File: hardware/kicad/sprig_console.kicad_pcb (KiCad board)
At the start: 2 copper layers, 139.7 x 64.8 mm, 42 parts, among them J1 1020_battery_holder, SW1 W, SW2 A, SW3 S, SW4 D, SW5 I, SW6 J, SW7 K, SW8 L, SW9 Slideswitch, U1 Adafruit_TFT_ST7735, U2 MAX98357AETE+, U5 Pico, X1 Simple_Addon_v2

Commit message: updated PCB
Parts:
- moved SW9 19.2 mm to (179.7, 61.2)
- moved C4 16.5 mm to (176.5, 73.1), turned to -90 degrees
- moved D3 14.2 mm to (179.1, 73.4), turned to 90 degrees
- moved X1 9.53 mm to (184.1, 74.3)
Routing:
- net Net-(J1-Pin_4): track 72.4 -> 104.9 mm
- net Net-(D3-K): track 16.1 -> 37.8 mm
- net GND: track 20.1 -> 31.8 mm
- net +3V3: track 59.3 -> 66.4 mm
- net Net-(D3-A): track 5.38 -> 12.5 mm
- net unconnected-(SW9-A-Pad1): track 0.00 -> 5.46 mm
- net GPIO1: track 19.6 -> 25.0 mm
- net GPIO0: track 14.3 -> 18.2 mm, vias 0 -> 1
- net GPIO3: track 12.8 -> 11.2 mm
- net GPIO2: track 13.4 -> 13.3 mm, vias 0 -> 2

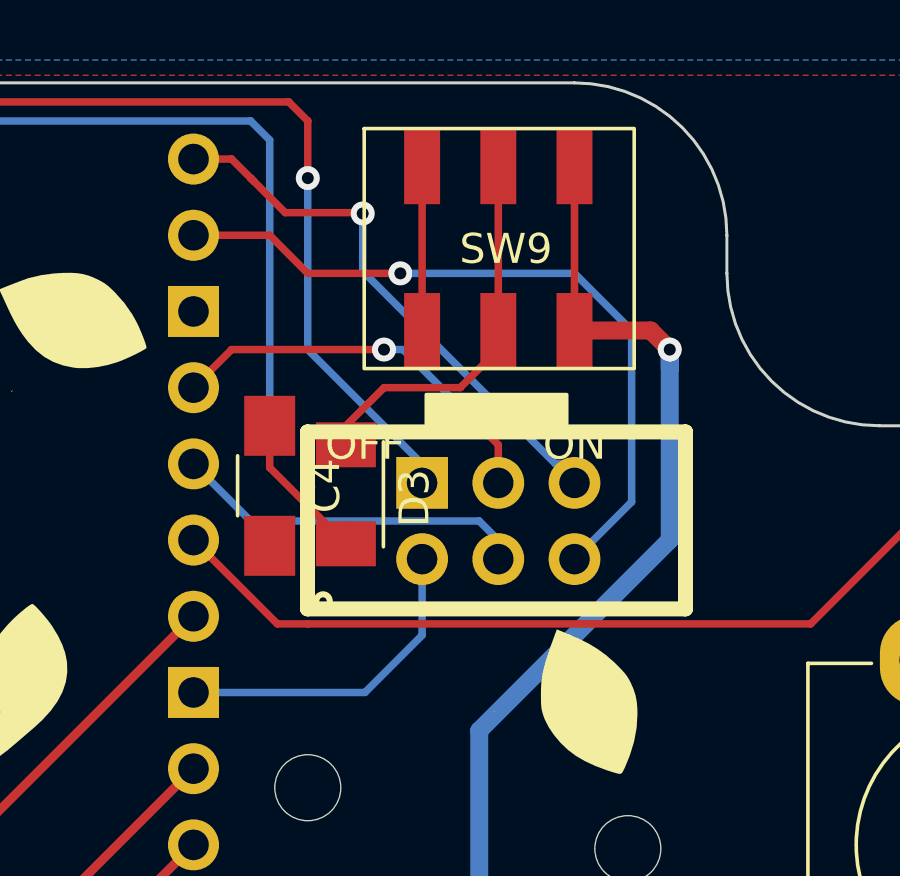
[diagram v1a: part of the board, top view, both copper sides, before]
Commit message: flipped connector to face other side
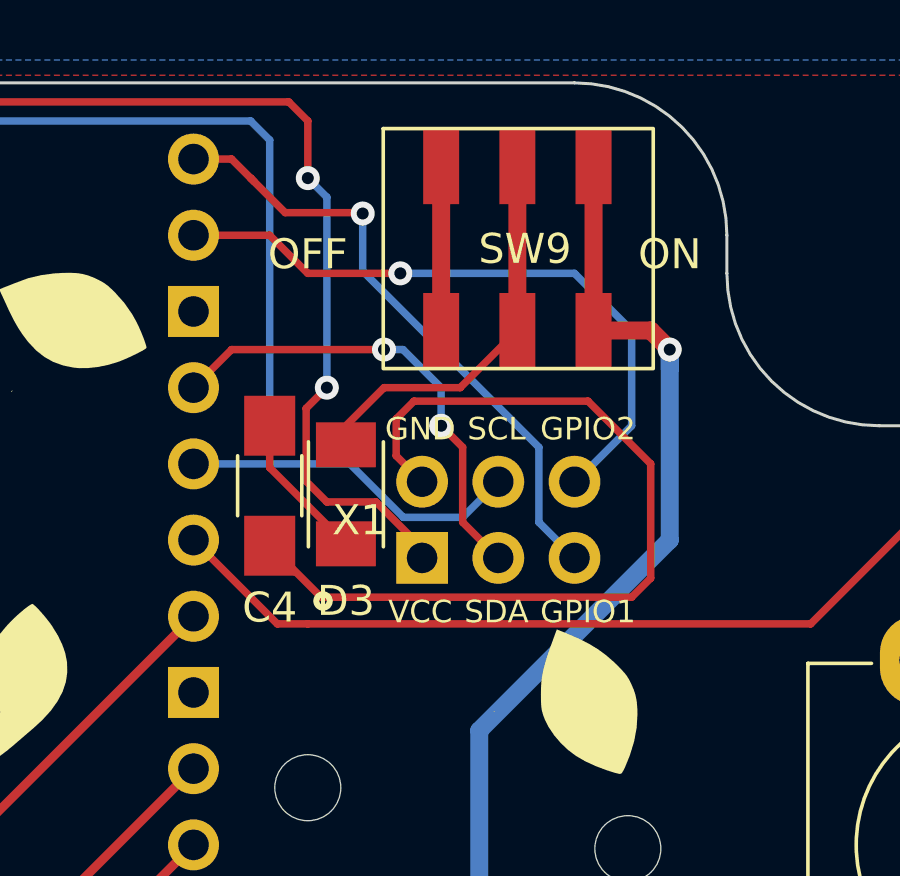
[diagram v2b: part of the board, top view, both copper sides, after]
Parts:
- X1: moved to B.Cu
- moved SW9 0.64 mm to (180.3, 61.2)
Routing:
- net GND: track 31.8 -> 49.7 mm
- net +3V3: track 66.4 -> 71.1 mm, vias 3 -> 4
- net GPIO0: track 18.2 -> 21.6 mm
- net GPIO1: track 25.0 -> 21.8 mm
- net GPIO2: track 13.3 -> 15.8 mm
- net Net-(J1-Pin_4): track 104.9 -> 104.3 mm
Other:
- board text removed: "GND"
- board text removed: "GP0"
- board text removed: "GP2"

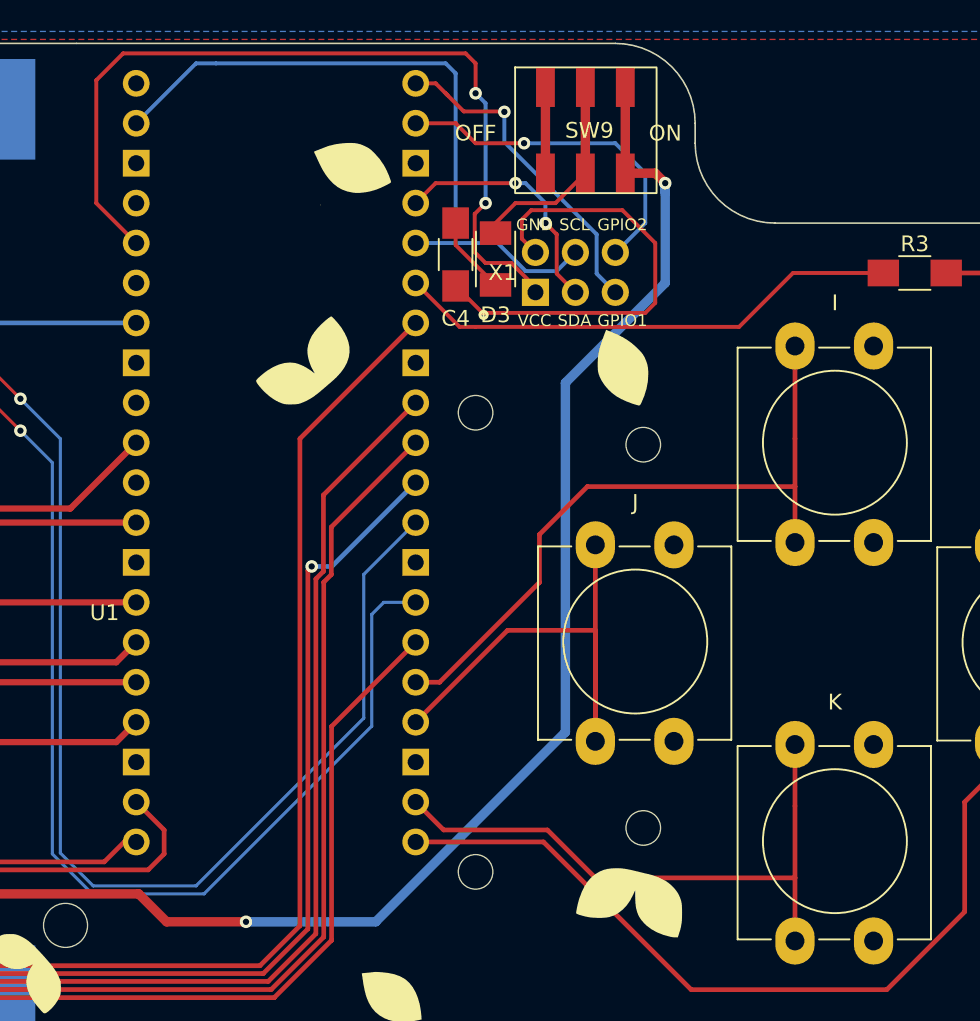
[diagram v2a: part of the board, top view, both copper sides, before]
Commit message: updated board design (moved SAO connector)
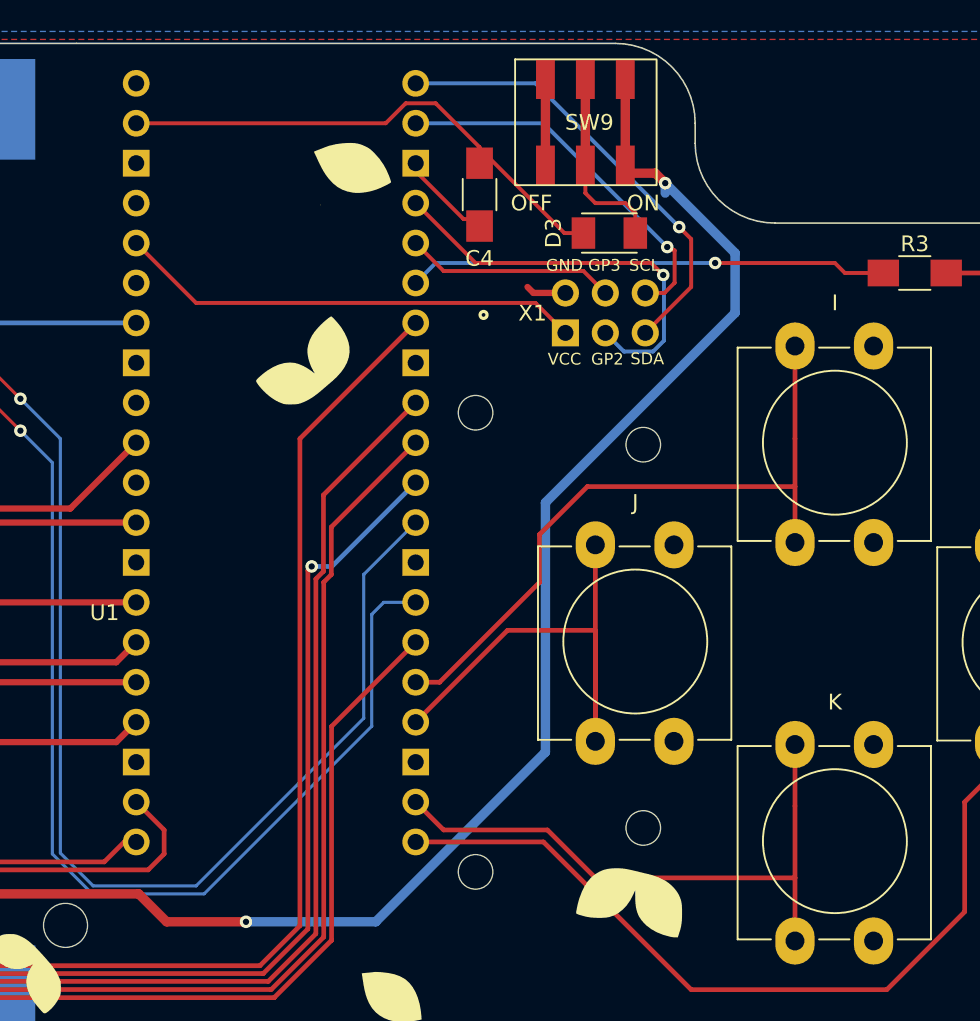
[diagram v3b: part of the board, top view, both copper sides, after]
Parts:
- moved D3 7.43 mm to (186.3, 71.8), turned to 0 degrees
- moved C4 4.10 mm to (178.1, 69.3)
- moved X1 3.21 mm to (186.0, 76.9)
- moved SW9 0.51 mm to (180.3, 60.7)
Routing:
- net +3V3: track 71.1 -> 46.6 mm, vias 4 -> 2
- net GND: track 49.7 -> 28.0 mm
- net GPIO2: track 15.8 -> 26.3 mm, vias 2 -> 1
- net GPIO0: track 21.6 -> 28.8 mm
- net Net-(D3-K): track 37.8 -> 32.4 mm
- net Net-(J1-Pin_4): track 104.3 -> 108.0 mm
- net GPIO1: track 21.8 -> 24.2 mm
- net GPIO3: track 11.4 -> 13.4 mm
- net LED_R: track 32.3 -> 31.4 mm, vias 0 -> 1
- net Net-(D3-A): track 12.5 -> 11.7 mm

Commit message: reorganize repo
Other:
- board text added: "sprighax v0.3"
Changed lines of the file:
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@@
     (fp_poly
       (pts
-        (xy -32.261953 14.424582)
-        (xy -31.962338 14.323591)
-        (xy -31.675465 14.169022)
-        (xy -31.397389 13.960043)
-        (xy -31.218679 13.793828)
-        (xy -31.097695 13.664151)
-        (xy -30.969346 13.512603)
-        (xy -30.854829 13.364661)
-        (xy -30.816273 13.310195)
-        (xy -30.717327 13.159996)
-        (xy -30.622706 13.007095)
-        (xy -30.537935 12.861402)
-        (xy -30.468539 12.732825)
-        (xy -30.420042 12.631272)
-        (xy -30.397968 12.566655)
-        (xy -30.397206 12.558517)
-        (xy -30.422986 12.508886)
-        (xy -30.494851 12.440646)
-        (xy -30.604592 12.358626)
-        (xy -30.743997 12.267655)
-        (xy -30.904857 12.172561)
-        (xy -31.07896 12.078173)
-        (xy -31.258097 11.989319)
-        (xy -31.434056 11.910827)
-        (xy -31.598627 11.847527)
-        (xy -31.616673 11.841365)
-        (xy -31.752667 11.796717)
-        (xy -31.861261 11.765485)
-        (xy -31.959487 11.744958)
-        (xy -32.064374 11.732426)
-        (xy -32.192952 11.725179)
-        (xy -32.362251 11.720508)
-        (xy -32.378347 11.720158)
-        (xy -32.615079 11.719087)
-        (xy -32.801004 11.726996)
-        (xy -32.932668 11.743713)
-        (xy -32.954947 11.748795)
-        (xy -33.233815 11.848087)
-        (xy -33.512579 12.000799)
-        (xy -33.784002 12.201644)
-        (xy -34.040845 12.445336)
-        (xy -34.253934 12.697423)
-        (xy -34.327646 12.799259)
-        (xy -34.421553 12.936304)
-        (xy -34.525327 13.093114)
-        (xy -34.628646 13.254243)
-        (xy -34.664917 13.312226)
-        (xy -34.916444 13.717467)
-        (xy -34.601004 13.894667)
-        (xy -34.395983 14.00724)
-        (xy -34.222182 14.095637)
-        (xy -34.061286 14.167991)
-        (xy -33.894981 14.232429)
-        (xy -33.704952 14.297084)
-        (xy -33.66678 14.309383)
-        (xy -33.276724 14.414394)
-        (xy -32.915199 14.469152)
-        (xy -32.578258 14.472825)
-      )
-      (stroke (width 0) (type solid)) (fill solid) (layer "B.SilkS"))
-    (fp_poly
-      (pts
         (xy 53.357871 18.808519)
         (xy 53.421407 18.77058)
@@
     (effects (font (size 1 1) (thickness 0.15)))
   )
+  (gr_text "sprighax v0.3" (at 132.842 122.936) (layer "F.SilkS")
+    (effects (font (size 1 1) (thickness 0.15)) (justify left bottom))
+  )
   (gr_text "ON\n" (at 188.468 69.85) (layer "F.SilkS")
